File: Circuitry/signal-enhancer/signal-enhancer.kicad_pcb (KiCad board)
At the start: 2 copper layers, 105.5 x 91.5 mm, 25 parts, among them J1 Conn_01x06_Pin, J2 Conn_01x06_Pin, U1 NE555P, U2 74HC14, U4 SN74LS74AN, U5 SN74LS74AN, U7 SN74LS74AN

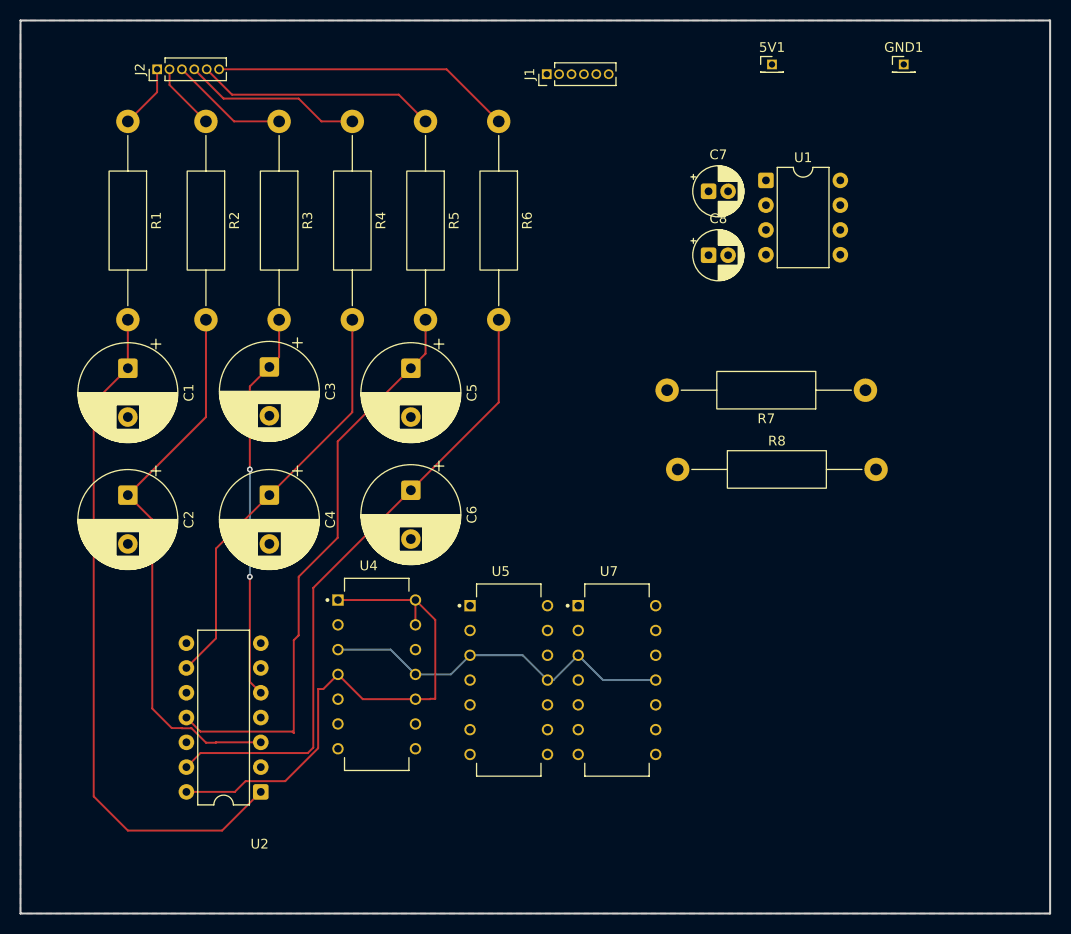
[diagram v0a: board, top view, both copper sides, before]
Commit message: Update PCB layout and connector footprints
Modified component values to include Ω symbols and moved value layers to F.SilkS for better visibility. Updated positions of several components and changed connector footprints from 1.27mm to 2.54mm pitch for J2 and related connectors. Added new backup and PCB zip files, removed obsolete autosave and lock files, and added new STL files for valve bracket and holder plate.
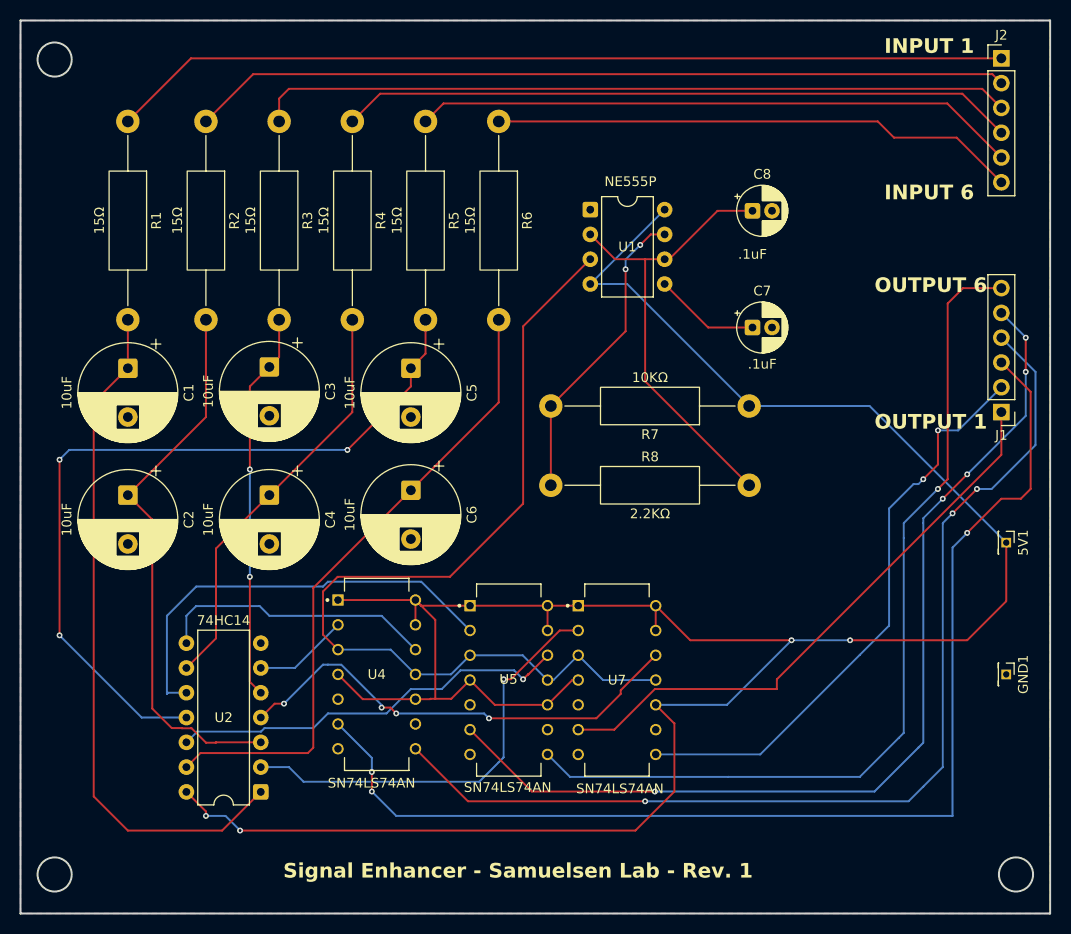
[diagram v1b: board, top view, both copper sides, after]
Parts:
- J1, J2: footprint Connector_PinHeader_1.27mm:PinHeader_1x06_P1.27mm_Vertical -> Connector_PinHeader_2.54mm:PinHeader_1x06_P2.54mm_Vertical
- R1, R2, R3, R4, R5, R6: value 15 -> 15Ω
- R7: value 10000 -> 10KΩ
- R8: value 2200 -> 2.2KΩ
- moved J2 86.5 mm to (134.5, 28.9), turned to 0 degrees
- moved GND1 63.4 mm to (135.0, 92.0), turned to -90 degrees
- moved J1 58.0 mm to (134.5, 65.1), turned to 180 degrees
- moved 5V1 54.6 mm to (135.0, 78.5), turned to -90 degrees
- moved U1 18.2 mm to (92.4, 44.4)
- moved C7 14.7 mm to (109.0, 56.5)
- moved R8 13.1 mm to (88.3, 72.6)
- moved R7 12.0 mm to (108.7, 64.5)
- moved C8 6.40 mm to (109.0, 44.5)
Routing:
- net /5V: track 56.6 -> 269.3 mm, vias 0 -> 4
- net /OUT_3: track 0.00 -> 121.1 mm, vias 0 -> 3
- net /OUT_4: track 0.00 -> 108.0 mm, vias 0 -> 3
- net /OUT_5: track 0.00 -> 100.6 mm, vias 0 -> 5
- net /OUT_6: track 0.00 -> 91.3 mm, vias 0 -> 1
- net /IN_1: track 6.58 -> 92.2 mm
- net /IN_2: track 6.89 -> 83.9 mm
- net /IN_3: track 12.2 -> 77.6 mm
- net /OUT_2: track 0.00 -> 60.1 mm, vias 0 -> 2
- net /OUT_1: track 0.00 -> 60.0 mm
- net /555_CLK: track 37.6 -> 96.3 mm
- net /IN_4: track 18.4 -> 69.3 mm
- net Net-(U7-2D): track 0.00 -> 48.0 mm, vias 0 -> 4
- net /pin_6_to_2: track 0.00 -> 47.3 mm
- net Net-(U5-1D): track 0.00 -> 44.6 mm
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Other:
- outline, holes or cut-outs redrawn
- board text added: "INPUT 1"
- board text added: "INPUT 6"
- board text added: "OUTPUT 1"
- board text added: "OUTPUT 6"
- board text added: "Signal Enhancer - Samuelsen Lab - Rev. 1"
